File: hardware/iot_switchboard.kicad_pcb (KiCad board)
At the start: 2 copper layers, 64.8 x 27.9 mm, 17 parts, among them IC1 ATTINY84-M, P1 CONN_01X05, P2 CONN_01X05, T1 CONN_01X01

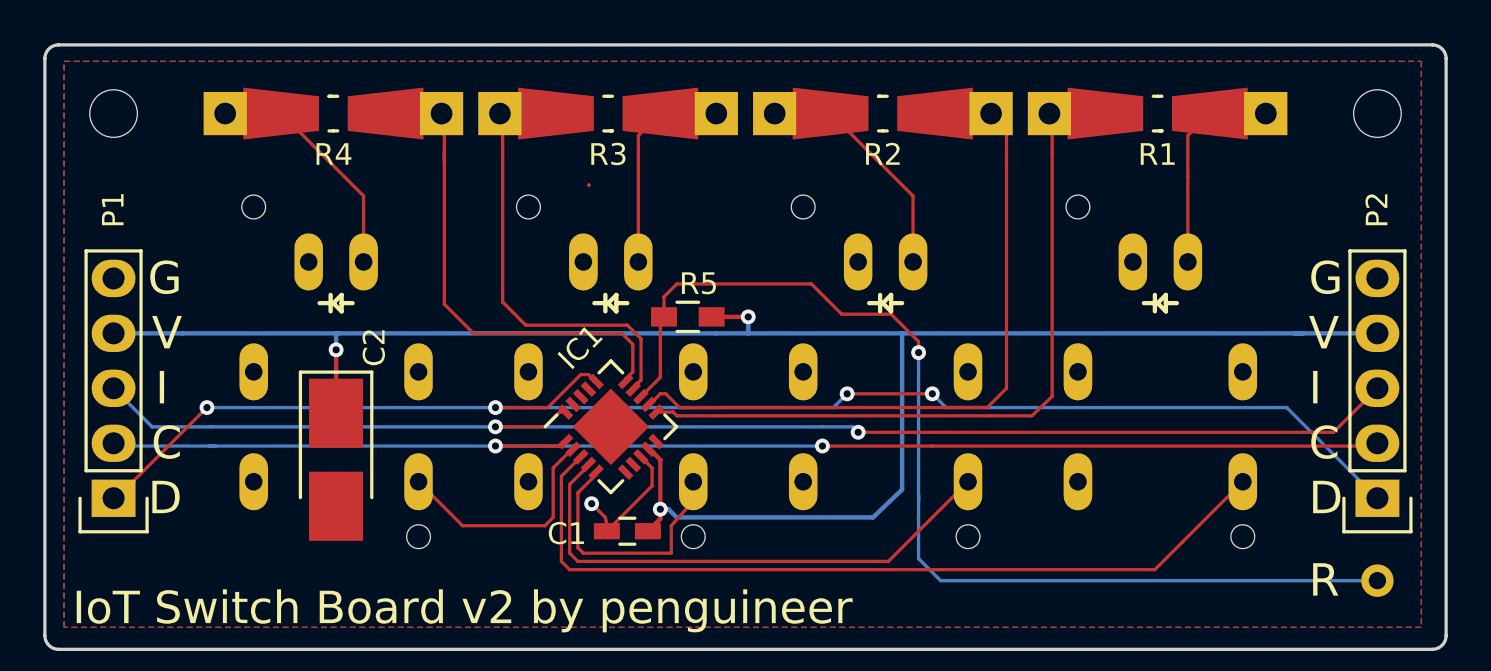
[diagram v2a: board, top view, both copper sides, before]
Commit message: Replace load capacitor by 0603 type
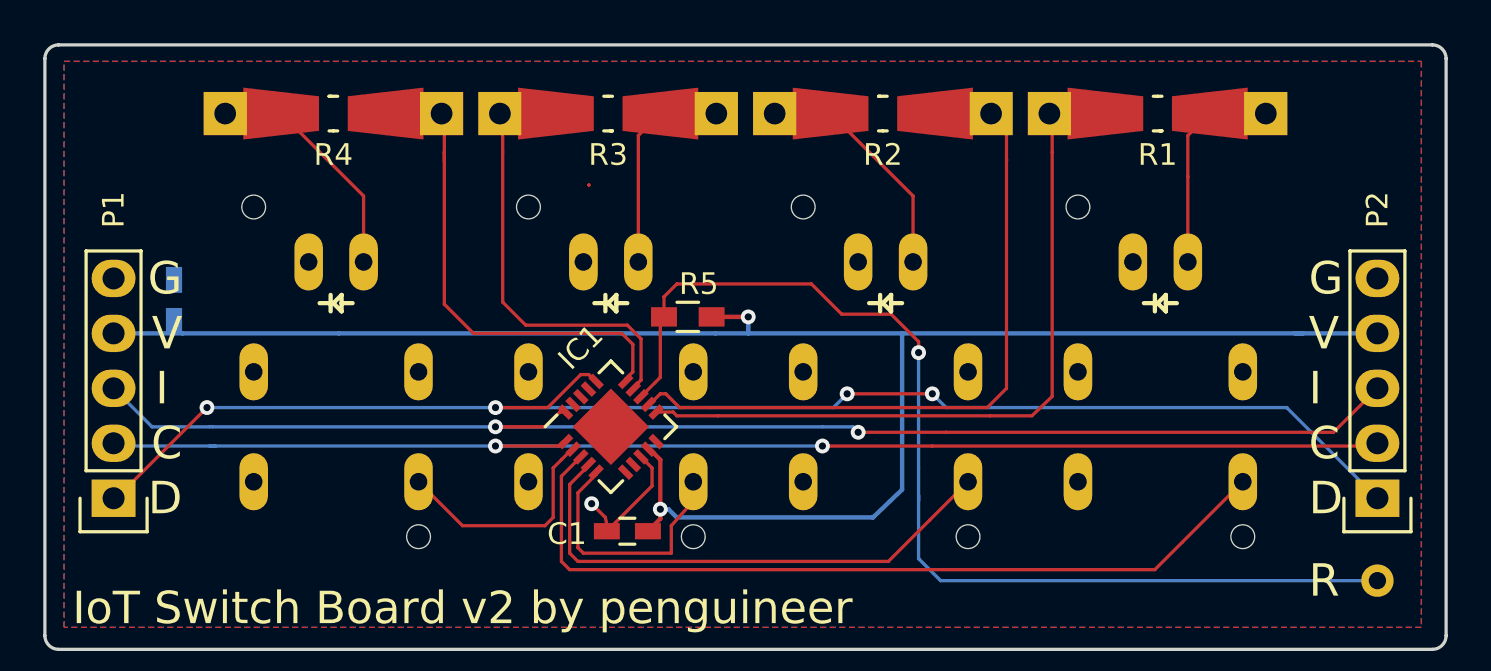
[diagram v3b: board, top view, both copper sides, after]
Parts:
- removed REF** (x2): MountingHole_2.2mm_M2_ISO14580, Mounting_Holes:MountingHole_2.2mm_M2_ISO14580
- C2: footprint Capacitors_Tantalum_SMD:Tantalum_Case-B_EIA-3528-21_Hand -> Capacitors_SMD:C_0603_HandSoldering; moved to B.Cu
- moved C2 10.5 mm to (166.1, 63.2), turned to 90 degrees
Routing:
- net VCC_IN: track 88.7 -> 85.6 mm, vias 3 -> 2
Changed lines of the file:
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@@
     (thickness 1.6)
     (drawings 44)
-    (tracks 204)
+    (tracks 202)
     (zones 0)
-    (modules 17)
+    (modules 15)
     (nets 19)
   )
@@
     )
   )
-  (module Capacitors_Tantalum_SMD:Tantalum_Case-B_EIA-3528-21_Hand (layer F.Cu)
-    (at 173.609 70.612 270)
-    (descr "Tantalum capacitor, Case B, EIA 3528-21, 3.5x2.8x1.9mm, Hand soldering footprint")
-    (tags "capacitor tantalum smd")
-    (attr smd)
-    (fp_text reference C2 (at -5.207 -1.778 270) (layer F.SilkS)
-      (effects (font (size 1 1) (thickness 0.15)))
-    )
-    (fp_text value 3u3 (at 0 3.15 270) (layer F.Fab)
-      (effects (font (size 1 1) (thickness 0.15)))
-    )
-    (fp_line (start -4.15 -1.75) (end -4.15 1.75) (layer F.CrtYd) (width 0.05))
-    (fp_line (start -4.15 1.75) (end 4.15 1.75) (layer F.CrtYd) (width 0.05))
-    (fp_line (start 4.15 1.75) (end 4.15 -1.75) (layer F.CrtYd) (width 0.05))
-    (fp_line (start 4.15 -1.75) (end -4.15 -1.75) (layer F.CrtYd) (width 0.05))
-    (fp_line (start -1.75 -1.4) (end -1.75 1.4) (layer F.Fab) (width 0.15))
-    (fp_line (start -1.75 1.4) (end 1.75 1.4) (layer F.Fab) (width 0.15))
-    (fp_line (start 1.75 1.4) (end 1.75 -1.4) (layer F.Fab) (width 0.15))
-    (fp_line (start 1.75 -1.4) (end -1.75 -1.4) (layer F.Fab) (width 0.15))
-    (fp_line (start -1.4 -1.4) (end -1.4 1.4) (layer F.Fab) (width 0.15))
-    (fp_line (start -1.225 -1.4) (end -1.225 1.4) (layer F.Fab) (width 0.15))
-    (fp_line (start -4.05 -1.65) (end 1.75 -1.65) (layer F.SilkS) (width 0.15))
-    (fp_line (start -4.05 1.65) (end 1.75 1.65) (layer F.SilkS) (width 0.15))
-    (fp_line (start -4.05 -1.65) (end -4.05 1.65) (layer F.SilkS) (width 0.15))
-    (pad 1 smd rect (at -2.15 0 270) (size 3.2 2.5) (layers F.Cu F.Paste F.Mask)
-      (net 1 VCC_IN))
-    (pad 2 smd rect (at 2.15 0 270) (size 3.2 2.5) (layers F.Cu F.Paste F.Mask)
-      (net 2 GND))
-    (model Capacitors_Tantalum_SMD.3dshapes/Tantalum_Case-B_EIA-3528-21.wrl
-      (at (xyz 0 0 0))
-      (scale (xyz 1 1 1))
-      (rotate (xyz 0 0 0))
-    )
-  )
   (module Capacitors_SMD:C_0603_HandSoldering (layer F.Cu)
     (at 187.071 73.914 180)
@@
       (net 4 RST))
   )
-  (module Mounting_Holes:MountingHole_2.2mm_M2_ISO14580 (layer F.Cu)
-    (at 163.322 54.61)
-    (descr "Mounting Hole 2.2mm, no annular, M2, ISO14580")
-    (tags "mounting hole 2.2mm no annular m2 iso14580")
-    (fp_text reference REF** (at 0 -2.9) (layer F.SilkS) hide
-      (effects (font (size 1 1) (thickness 0.15)))
-    )
-    (fp_text value MountingHole_2.2mm_M2_ISO14580 (at 0 2.9) (layer F.Fab) hide
-      (effects (font (size 1 1) (thickness 0.15)))
-    )
-    (fp_circle (center 0 0) (end 1.9 0) (layer Cmts.User) (width 0.15))
-    (fp_circle (center 0 0) (end 2.15 0) (layer F.CrtYd) (width 0.05))
-    (pad 1 np_thru_hole circle (at 0 0) (size 2.2 2.2) (drill 2.2) (layers *.Cu *.Mask))
-  )
-  (module Mounting_Holes:MountingHole_2.2mm_M2_ISO14580 (layer F.Cu)
-    (at 221.742 54.61)
-    (descr "Mounting Hole 2.2mm, no annular, M2, ISO14580")
-    (tags "mounting hole 2.2mm no annular m2 iso14580")
-    (fp_text reference REF** (at 0 -2.9) (layer F.SilkS) hide
-      (effects (font (size 1 1) (thickness 0.15)))
-    )
-    (fp_text value MountingHole_2.2mm_M2_ISO14580 (at 0 2.9) (layer F.Fab) hide
-      (effects (font (size 1 1) (thickness 0.15)))
-    )
-    (fp_circle (center 0 0) (end 1.9 0) (layer Cmts.User) (width 0.15))
-    (fp_circle (center 0 0) (end 2.15 0) (layer F.CrtYd) (width 0.05))
-    (pad 1 np_thru_hole circle (at 0 0) (size 2.2 2.2) (drill 2.2) (layers *.Cu *.Mask))
+  (module Capacitors_SMD:C_0603_HandSoldering (layer B.Cu)
+    (at 166.116 63.246 90)
+    (descr "Capacitor SMD 0603, hand soldering")
+    (tags "capacitor 0603")
+    (attr smd)
+    (fp_text reference C2 (at 3.302 0 90) (layer B.SilkS)
+      (effects (font (size 1 1) (thickness 0.15)) (justify mirror))
+    )
+    (fp_text value 3u3 (at 0 -1.9 90) (layer B.Fab)
+      (effects (font (size 1 1) (thickness 0.15)) (justify mirror))
+    )
+    (fp_line (start -0.8 -0.4) (end -0.8 0.4) (layer B.Fab) (width 0.15))
+    (fp_line (start 0.8 -0.4) (end -0.8 -0.4) (layer B.Fab) (width 0.15))
+    (fp_line (start 0.8 0.4) (end 0.8 -0.4) (layer B.Fab) (width 0.15))
+    (fp_line (start -0.8 0.4) (end 0.8 0.4) (layer B.Fab) (width 0.15))
+    (fp_line (start -1.85 0.75) (end 1.85 0.75) (layer B.CrtYd) (width 0.05))
+    (fp_line (start -1.85 -0.75) (end 1.85 -0.75) (layer B.CrtYd) (width 0.05))
+    (fp_line (start -1.85 0.75) (end -1.85 -0.75) (layer B.CrtYd) (width 0.05))
+    (fp_line (start 1.85 0.75) (end 1.85 -0.75) (layer B.CrtYd) (width 0.05))
+    (fp_line (start -0.35 0.6) (end 0.35 0.6) (layer B.SilkS) (width 0.15))
+    (fp_line (start 0.35 -0.6) (end -0.35 -0.6) (layer B.SilkS) (width 0.15))
+    (pad 1 smd rect (at -0.95 0 90) (size 1.2 0.75) (layers B.Cu B.Paste B.Mask)
+      (net 1 VCC_IN))
+    (pad 2 smd rect (at 0.95 0 90) (size 1.2 0.75) (layers B.Cu B.Paste B.Mask)
+      (net 2 GND))
+    (model Capacitors_SMD.3dshapes/C_0603_HandSoldering.wrl
+      (at (xyz 0 0 0))
+      (scale (xyz 1 1 1))
+      (rotate (xyz 0 0 0))
+    )
   )
   (gr_line (start 211.963 63.373) (end 212.471 63.373) (angle 90) (layer F.SilkS) (width 0.2))
@@
   (segment (start 185.293 57.913598) (end 185.293 57.912) (width 0.1524) (layer F.Cu) (net 0))
   (segment (start 185.293 57.912) (end 185.293 57.912) (width 0.1524) (layer F.Cu) (net 0))
-  (segment (start 173.609 68.462) (end 173.609 65.532) (width 0.2032) (layer F.Cu) (net 1))
-  (segment (start 173.609 64.77) (end 173.736 64.77) (width 0.2032) (layer B.Cu) (net 1))
-  (segment (start 173.609 65.532) (end 173.609 64.77) (width 0.2032) (layer B.Cu) (net 1))
-  (via (at 173.609 65.532) (size 0.6858) (drill 0.3302) (layers F.Cu B.Cu) (net 1))
+  (segment (start 166.116 64.069) (end 166.116 64.77) (width 0.2032) (layer B.Cu) (net 1))
   (segment (start 188.595 72.898) (end 188.976 72.898) (width 0.2032) (layer B.Cu) (net 1))
   (via (at 188.595 72.898) (size 0.6858) (drill 0.3302) (layers F.Cu B.Cu) (net 1))
@@
   (segment (start 188.976 72.898) (end 189.357 73.279) (width 0.2032) (layer B.Cu) (net 1))
   (segment (start 221.742 64.77) (end 217.932 64.77) (width 0.2032) (layer B.Cu) (net 1))
-  (segment (start 163.322 64.77) (end 166.497 64.77) (width 0.2032) (layer B.Cu) (net 1))
+  (segment (start 163.322 64.77) (end 166.116 64.77) (width 0.2032) (layer B.Cu) (net 1))
+  (segment (start 166.116 64.77) (end 166.497 64.77) (width 0.2032) (layer B.Cu) (net 1))
   (segment (start 166.497 64.77) (end 173.736 64.77) (width 0.2032) (layer B.Cu) (net 1))
   (segment (start 173.736 64.77) (end 188.595 64.77) (width 0.2032) (layer B.Cu) (net 1))

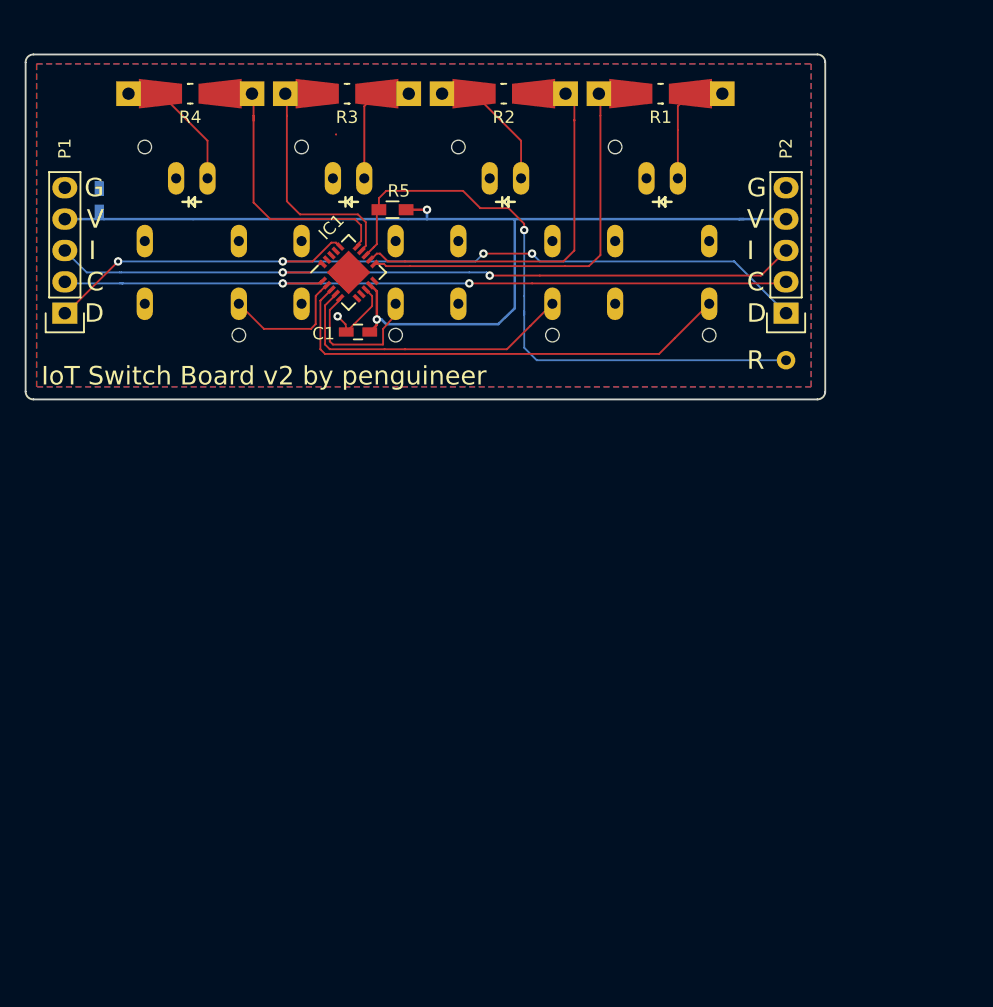
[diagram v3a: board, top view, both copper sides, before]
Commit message: Reduce to 2 switches and adapt outline
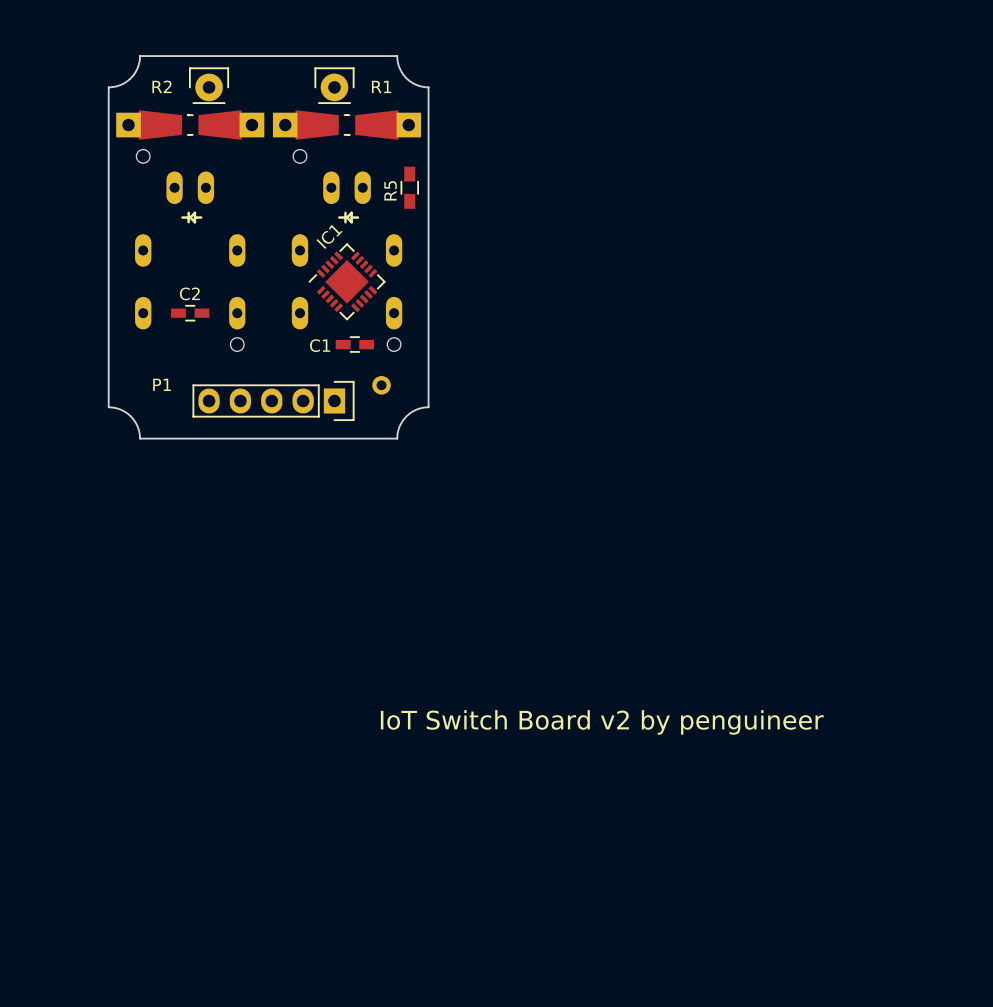
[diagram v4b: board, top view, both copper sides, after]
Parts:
- removed P2: CONN_01X05, Socket_Strips:Socket_Strip_Straight_1x05
- removed R3, R4: R, Resistors_Universal:Resistor_SMD+THTuniversal_0805to1206_RM10_HandSoldering
- removed S3, S4: n39-SWITCH_SRKL_LED, n39-SWITCH_SRKL_LED
- added REF**: Pin_Header_Straight_1x01, Pin_Headers:Pin_Header_Straight_1x01, F.Cu at (175.0, 54.1)
- added REF**: Pin_Header_Straight_1x01, Pin_Headers:Pin_Header_Straight_1x01, F.Cu at (185.2, 54.1)
- C2: moved to F.Cu
- P1: footprint Socket_Strips:Socket_Strip_Straight_1x05 -> Pin_Headers:Pin_Header_Straight_1x05
- moved T1 32.8 mm to (189.0, 78.2)
- moved S1 25.5 mm to (186.2, 67.3)
- moved S2 25.5 mm to (173.5, 67.3)
- moved R1 25.5 mm to (186.2, 57.1)
- moved R2 25.5 mm to (173.5, 57.1)
- moved P1 23.0 mm to (185.2, 79.5), turned to 270 degrees
- moved C2 11.7 mm to (173.5, 72.4), turned to 180 degrees
- moved R5 2.26 mm to (191.3, 62.2), turned to 90 degrees
- moved C1 1.05 mm to (186.8, 74.9)
- moved IC1 0.77 mm to (186.2, 69.8)
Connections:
- IC1 pad 14: LED3 -> (no net)
- IC1 pad 15: LED4 -> (no net)
- IC1 pad 2: SW4 -> (no net)
- IC1 pad 5: SW3 -> (no net)
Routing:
- net VCC_IN: track 85.6 -> 0.00 mm, vias 2 -> 0
- net SDA: track 67.8 -> 0.00 mm, vias 4 -> 0
- net INT: track 63.7 -> 0.00 mm, vias 2 -> 0
- net SCL: track 62.3 -> 0.00 mm, vias 2 -> 0
- net RST: track 50.1 -> 0.00 mm, vias 1 -> 0
- net SW1: track 38.5 -> 0.00 mm
- net LED1: track 34.2 -> 0.00 mm
- net LED2: track 33.0 -> 0.00 mm
- net SW2: track 24.8 -> 0.00 mm
- net LED4: track 23.2 -> 0.00 mm
- net LED3: track 20.7 -> 0.00 mm
- net SW3: track 12.0 -> 0.00 mm
- net Net-(R4-Pad1): track 11.0 -> 0.00 mm
- net Net-(R2-Pad1): track 11.0 -> 0.00 mm
- net SW4: track 10.8 -> 0.00 mm
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- removed copper zone on B.Cu, net GND
- removed copper zone on F.Cu, net GND
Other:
- board size 64.8 x 27.9 mm -> 25.9 x 31 mm
- board text removed: "C"
- board text removed: "D"
- board text removed: "G"
- board text removed: "I"
- board text removed: "R"
- board text removed: "V"

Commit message: New Layout
Yeah!
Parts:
- removed the REF** at (175.0, 54.1)
- removed the REF** at (185.2, 54.1)
- added R3: 10K, Resistors_SMD:R_0603_HandSoldering, F.Cu at (179.6, 65.8)
- added R4: 0, Resistors_SMD:R_0402, F.Cu at (186.9, 76.5)
- added R6: 0, Resistors_SMD:R_0402, F.Cu at (189.5, 76.5)
- added REF**: MountingHole_2.2mm_M2, Mounting_Holes:MountingHole_2.2mm_M2, F.Cu at (190.5, 53.8)
- added REF**: MountingHole_2.2mm_M2, Mounting_Holes:MountingHole_2.2mm_M2, F.Cu at (169.2, 53.8)
- added REF**: MountingHole_2.2mm_M2, Mounting_Holes:MountingHole_2.2mm_M2, F.Cu at (169.4, 80.0)
- added REF**: MountingHole_2.2mm_M2, Mounting_Holes:MountingHole_2.2mm_M2, F.Cu at (190.2, 80.0)
- added REF**: SolderWirePad_single_1mmDrill, Wire_Pads:SolderWirePad_single_1mmDrill, F.Cu at (175.0, 54.1)
- added REF**: SolderWirePad_single_1mmDrill, Wire_Pads:SolderWirePad_single_1mmDrill, F.Cu at (185.2, 54.1)
- added REF***: OSHW-Logo2_7.3x6mm_SilkScreen, Symbols:OSHW-Logo2_7.3x6mm_SilkScreen, F.Cu at (173.5, 67.6)
- R5: value 10K -> 0; footprint Resistors_SMD:R_0603_HandSoldering -> Resistors_SMD:R_0402
- moved T1 25.7 mm to (180.1, 54.1)
- moved R5 14.5 mm to (188.2, 76.5)
- moved C1 10.3 mm to (188.2, 64.8), turned to 0 degrees
- turned IC1 to 135 degrees
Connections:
- IC1 pad 15: (no net) -> SW2
- IC1 pad 2: (no net) -> Net-(IC1-Pad2)
- IC1 pad 3: SW1 -> Net-(IC1-Pad3)
- IC1 pad 4: SW2 -> Net-(IC1-Pad4)
- IC1 pad 5: (no net) -> SW1
- P1 pad 1: SDA -> SCL
- P1 pad 2: SCL -> SDA
- R5 pad 1: VCC_IN -> GND
- R5 pad 2: RST -> Net-(IC1-Pad3)
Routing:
- net VCC_IN: track 0.00 -> 32.2 mm, vias 0 -> 2
- net RST: track 0.00 -> 24.1 mm, vias 0 -> 1
- net LED2: track 0.00 -> 16.3 mm
- net LED1: track 0.00 -> 15.0 mm
- net INT: track 0.00 -> 9.80 mm, vias 0 -> 2
- net SDA: track 0.00 -> 9.64 mm
- net Net-(R2-Pad1): track 0.00 -> 9.19 mm
- net SCL: track 0.00 -> 8.54 mm
- net SW2: track 0.00 -> 8.51 mm
- net Net-(R1-Pad1): track 0.00 -> 8.14 mm
- net Net-(IC1-Pad4): track 0.00 -> 5.80 mm
- net Net-(IC1-Pad3): track 0.00 -> 5.03 mm
- net Net-(IC1-Pad2): track 0.00 -> 4.93 mm
- net GND: track 0.00 -> 4.60 mm
- net SW1: track 0.00 -> 2.57 mm
- added copper zone on B.Cu, net GND
- added copper zone on F.Cu, net GND
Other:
- board text added: "Addr"
- board text added: "GND"
- board text added: "I2C"
- board text added: "INT"
- board text added: "RST"
- board text added: "SCL"
- board text added: "SDA"
- board text added: "Tapper Rev. 2"
- board text added: "Tapper Rev. 2 by penguineer"
- board text added: "VCC"
- board text removed: "IoT Switch Board v2 by penguineer"
